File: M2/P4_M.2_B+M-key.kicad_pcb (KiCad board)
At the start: 4 copper layers, 22 x 42 mm, 79 parts, among them IC1 XT25F128FWOIGT-W, IC2 TPS563202DRLR, IC4 TPS563202DRLR, J1 Micro_SD_Card_Det2, J2 USB_C_Receptacle_USB2.0_16P, Q2 MMDT2222A, U2 ESP32-P4NRW16, U5 CH340K, Y1 32KHz, Y2 40MHz

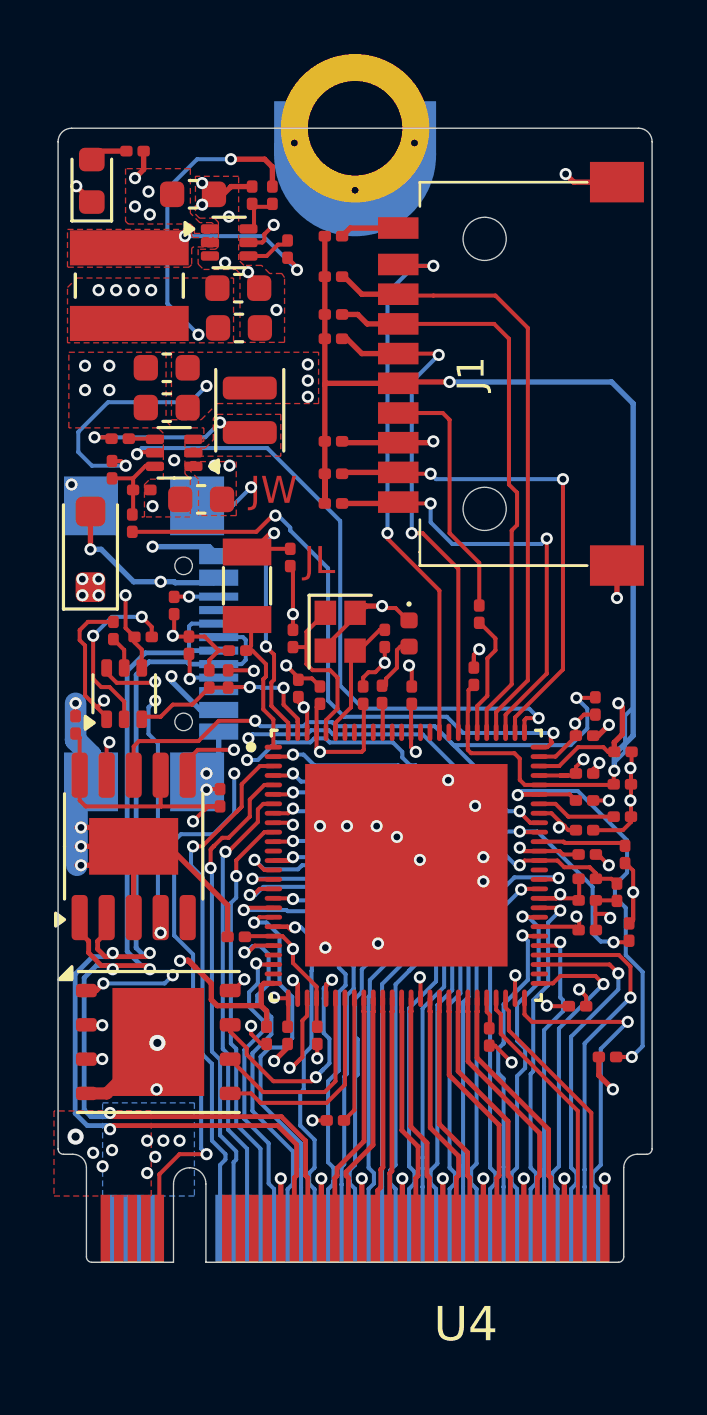
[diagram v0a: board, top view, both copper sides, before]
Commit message: fix: component positions & 3dmodels
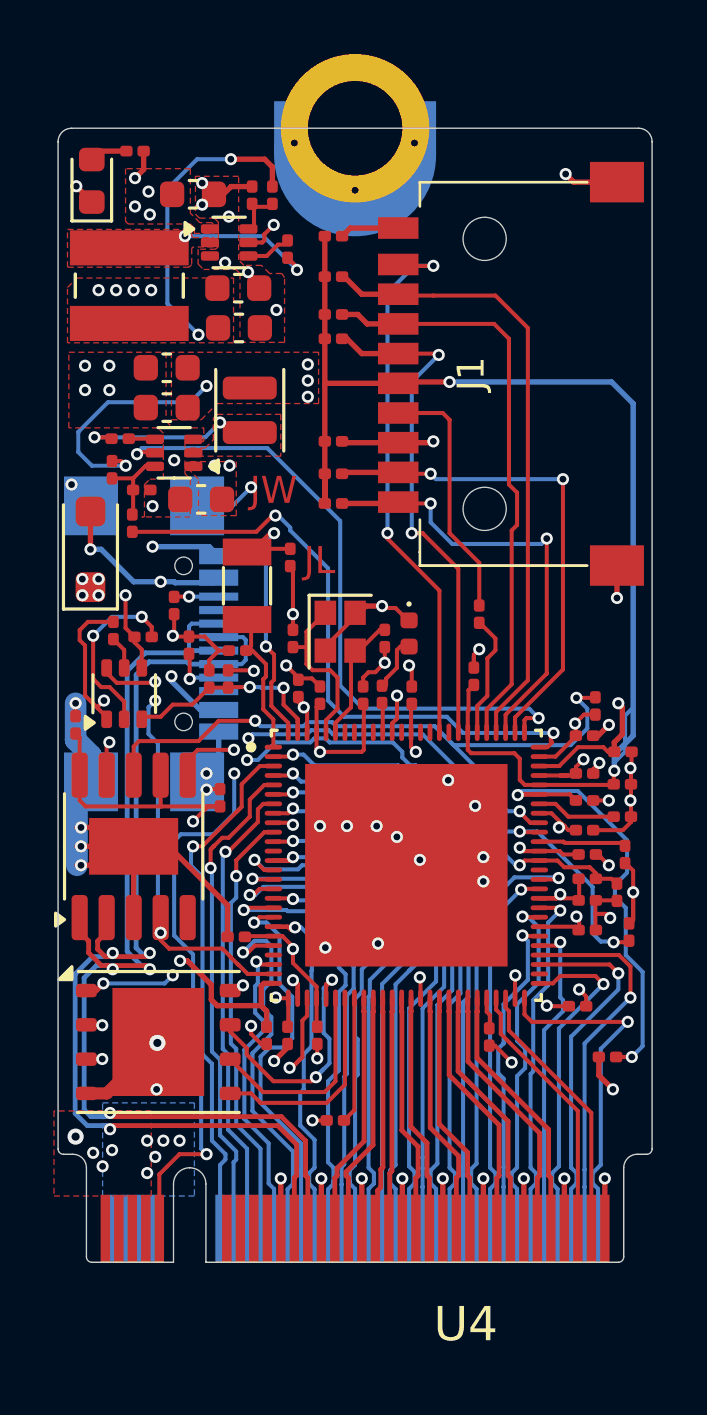
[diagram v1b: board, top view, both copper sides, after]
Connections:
- U2 pad 25: unconnected-(U2A-GPIO23-Pad25) -> /DTR
- U2 pad 93: unconnected-(U2A-GPIO50-Pad93) -> /RTS
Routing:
- net /RTS: track 16.2 -> 29.2 mm, vias 2 -> 3
- net /DTR: track 16.3 -> 21.8 mm

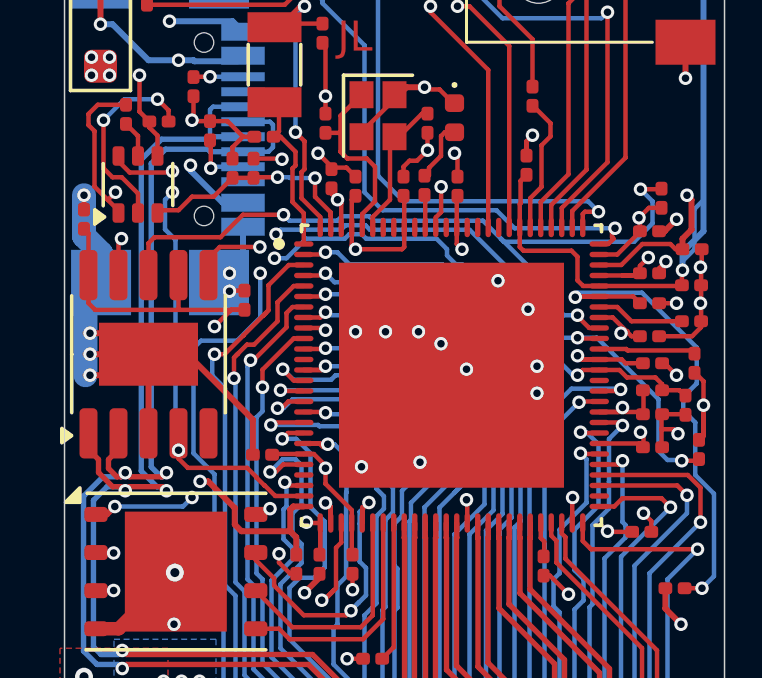
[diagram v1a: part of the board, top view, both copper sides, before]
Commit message: fix: revert m2 changes
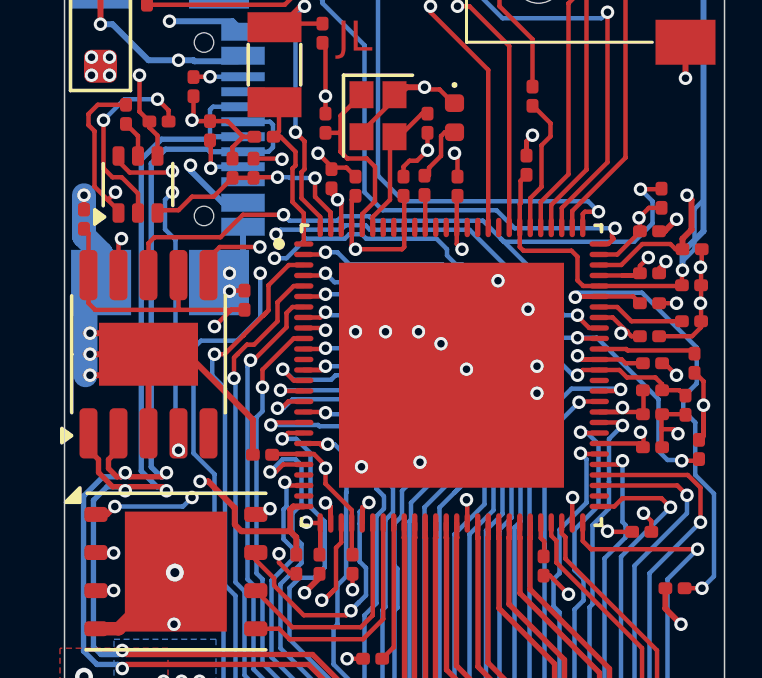
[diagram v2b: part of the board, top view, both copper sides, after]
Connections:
- U2 pad 25: /DTR -> unconnected-(U2A-GPIO23-Pad25)
- U2 pad 93: /RTS -> unconnected-(U2A-GPIO50-Pad93)
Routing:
- net /RTS: track 29.2 -> 16.2 mm, vias 3 -> 2
- net /DTR: track 21.8 -> 16.3 mm
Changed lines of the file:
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@@
 	(net 115 "/SD_DATA1")
 	(net 116 "/SD_DATA2")
+	(net 117 "unconnected-(U2A-GPIO23-Pad25)")
+	(net 118 "unconnected-(U2A-GPIO50-Pad93)")
 	(footprint "Resistor_SMD:R_0201_0603Metric"
 		(layer "F.Cu")
@@
 			(layers "F.Cu" "F.Paste")
 			(roundrect_rratio 0.5)
-			(net 34 "/DTR")
+			(net 117 "unconnected-(U2A-GPIO23-Pad25)")
 			(pinfunction "GPIO23")
-			(pintype "bidirectional")
+			(pintype "bidirectional+no_connect")
 			(solder_mask_margin 0.1)
 			(solder_paste_margin 0)
@@
 			(layers "F.Cu" "F.Paste")
 			(roundrect_rratio 0.5)
-			(net 35 "/RTS")
+			(net 118 "unconnected-(U2A-GPIO50-Pad93)")
 			(pinfunction "GPIO50")
-			(pintype "bidirectional")
+			(pintype "bidirectional+no_connect")
 			(solder_mask_margin 0.1)
 			(solder_paste_margin 0)
@@
 	)
 	(segment
-		(start 141.3 114.074999)
-		(end 141.3 113.2375)
-		(width 0.15)
-		(layer "F.Cu")
-		(net 34)
-	)
-	(segment
-		(start 145.475 115.325)
-		(end 144.525 115.325)
-		(width 0.15)
-		(layer "F.Cu")
-		(net 34)
-	)
-	(segment
-		(start 143.899 114.711811)
-		(end 143.899 114.699)
-		(width 0.15)
-		(layer "F.Cu")
-		(net 34)
-	)
-	(segment
 		(start 138.943906 105.456094)
 		(end 139.2 105.2)
@@
 	)
 	(segment
-		(start 144.176 114.976)
-		(end 144.163189 114.976)
-		(width 0.15)
-		(layer "F.Cu")
-		(net 34)
-	)
-	(segment
 		(start 139.3 105.812189)
 		(end 139.3 105.8925)
@@
 	)
 	(segment
-		(start 144.163189 114.976)
-		(end 143.899 114.711811)
-		(width 0.15)
-		(layer "F.Cu")
-		(net 34)
-	)
-	(segment
 		(start 138.607893 102.285)
 		(end 139.55 102.285)
@@
 	)
 	(segment
-		(start 144.525 115.325)
-		(end 144.176 114.976)
-		(width 0.15)
-		(layer "F.Cu")
-		(net 34)
-	)
-	(segment
-		(start 141.612367 114.387366)
-		(end 141.3 114.074999)
-		(width 0.15)
-		(layer "F.Cu")
-		(net 34)
-	)
-	(segment
 		(start 138.5 105.012189)
 		(end 138.943906 105.456094)
@@
 	)
 	(segment
-		(start 143.899 114.699)
-		(end 143.587366 114.387366)
-		(width 0.15)
-		(layer "F.Cu")
-		(net 34)
-	)
-	(segment
 		(start 138.3 102.962189)
 		(end 138.5 103.162189)
@@
 		(net 34)
 	)
-	(segment
-		(start 143.587366 114.387366)
-		(end 141.612367 114.387366)
-		(width 0.15)
-		(layer "F.Cu")
-		(net 34)
-	)
 	(via
 		(at 141.3 113.8)
@@
 	)
 	(segment
-		(start 149.875 106.375)
-		(end 149.875 106.040614)
-		(width 0.15)
-		(layer "F.Cu")
-		(net 35)
-	)
-	(segment
 		(start 142.5 107.2)
 		(end 142.674998 107.025002)
@@
 		(net 35)
 	)
-	(segment
-		(start 150.054554 105.86106)
-		(end 150.054554 105.01721)
-		(width 0.15)
-		(layer "F.Cu")
-		(net 35)
-	)
-	(segment
-		(start 149.875 106.040614)
-		(end 150.054554 105.86106)
-		(width 0.15)
-		(layer "F.Cu")
-		(net 35)
-	)
 	(via
 		(at 140 101.3)
@@
 		(net 35)
 	)
-	(via
-		(at 150.054554 105.01721)
-		(size 0.45)
-		(drill 0.25)
-		(layers "F.Cu" "B.Cu")
-		(net 35)
-	)
-	(segment
-		(start 141.107531 101.3)
-		(end 140 101.3)
-		(width 0.15)
-		(layer "In1.Cu")
-		(net 35)
-	)
 	(segment
 		(start 138.749 107.049)
@@
 	)
 	(segment
-		(start 142.407531 102.6)
-		(end 141.107531 101.3)
-		(width 0.15)
-		(layer "In1.Cu")
-		(net 35)
-	)
-	(segment
 		(start 144.012767 107.025002)
 		(end 143.841771 107.195998)
@@
 		(width 0.15)
 		(layer "In1.Cu")
-		(net 35)
-	)
-	(segment
-		(start 147.637344 102.6)
-		(end 142.407531 102.6)
-		(width 0.15)
-		(layer "In1.Cu")
-		(net 35)
-	)
-	(segment
-		(start 150.054554 105.01721)
-		(end 147.637344 102.6)
-		(width 0.15)
-		(layer "In1.Cu")

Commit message: Final Push M.2
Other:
- board text added: "DESIGN BY: JDJ, JW."
- board text added: "JDJ"
- board text added: "NOT A STANDARD M.2 CARD!"
- board text removed: "JL"
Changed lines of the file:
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@@
 			(at 0 5.645 90)
 			(layer "B.SilkS")
+			(hide yes)
 			(effects
 				(font
@@
 		)
 	)
-	(gr_text "JL"
+	(gr_text "JDJ"
 		(at 146.6 100.6 0)
 		(layer "F.Cu")
@@
 		)
 	)
+	(gr_text "NOT A STANDARD M.2 CARD!"
+		(at 149.25 91 90)
+		(layer "B.SilkS")
+		(effects
+			(font
+				(size 1.2 1.2)
+				(thickness 0.24)
+				(bold yes)
+			)
+			(justify left bottom mirror)
+		)
+	)
+	(gr_text "DESIGN BY: JDJ, JW."
+		(at 158.75 85.25 0)
+		(layer "B.SilkS")
+		(effects
+			(font
+				(size 0.4 0.4)
+				(thickness 0.08)
+				(bold yes)
+			)
+			(justify left bottom mirror)
+		)
+	)

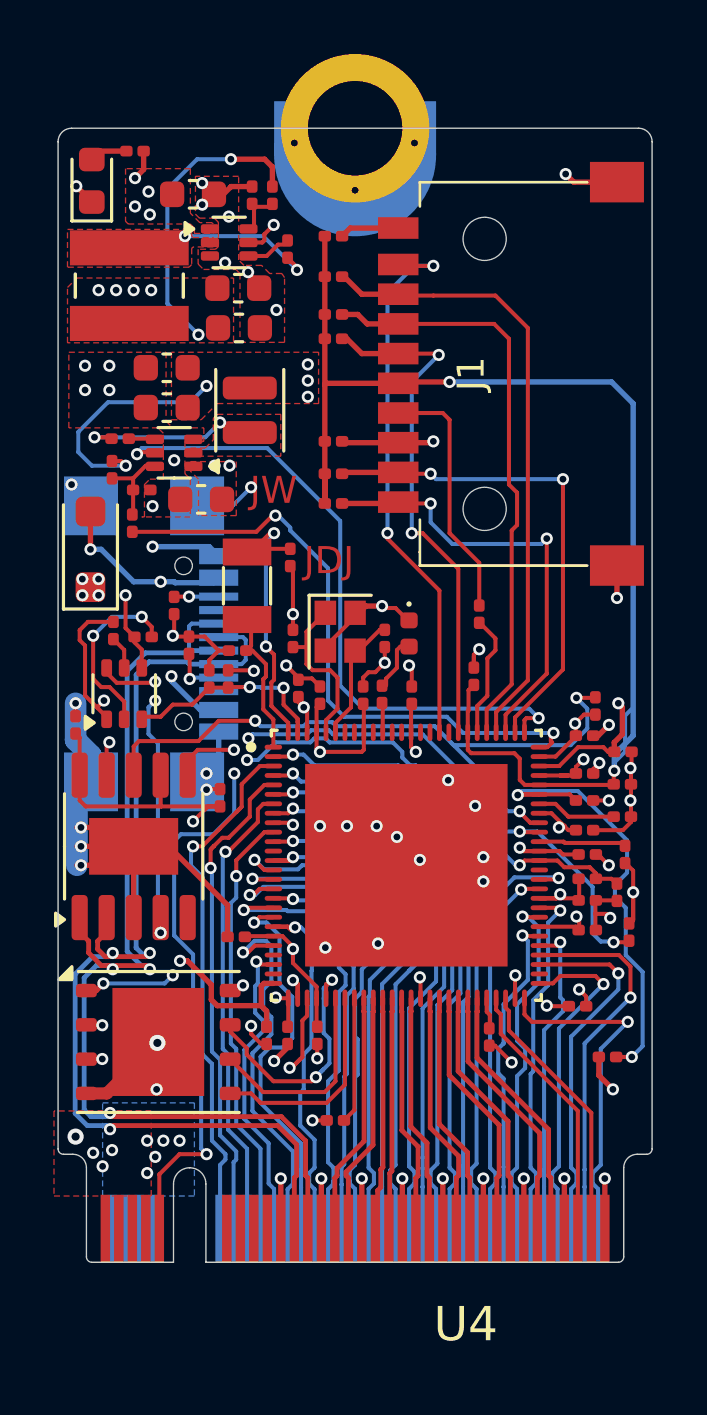
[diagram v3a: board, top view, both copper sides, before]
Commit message: Fixed esp_en issue
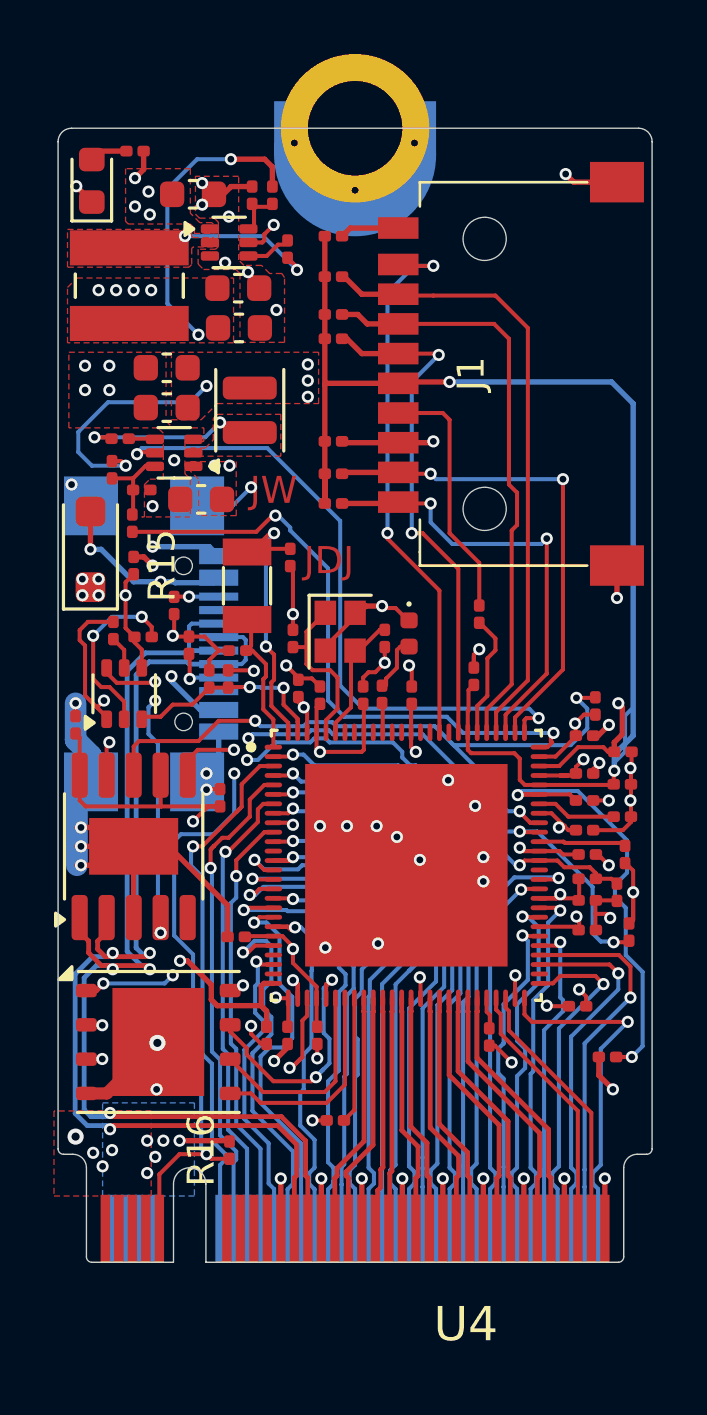
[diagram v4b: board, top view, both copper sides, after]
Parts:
- added R15: 1k, Resistor_SMD:R_0201_0603Metric, F.Cu at (140.3, 100.2)
- added R16: 0, Resistor_SMD:R_0201_0603Metric, F.Cu at (143.8, 121.8)
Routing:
- net /3.3V: track 57.7 -> 61.0 mm, vias 24 -> 25
- net /RTC: track 25.7 -> 26.7 mm
- net /RTS: track 16.2 -> 17.1 mm
